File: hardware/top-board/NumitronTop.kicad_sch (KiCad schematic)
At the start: 11 parts, among them J1 61201621621, U1 AP7361C-Y5-13

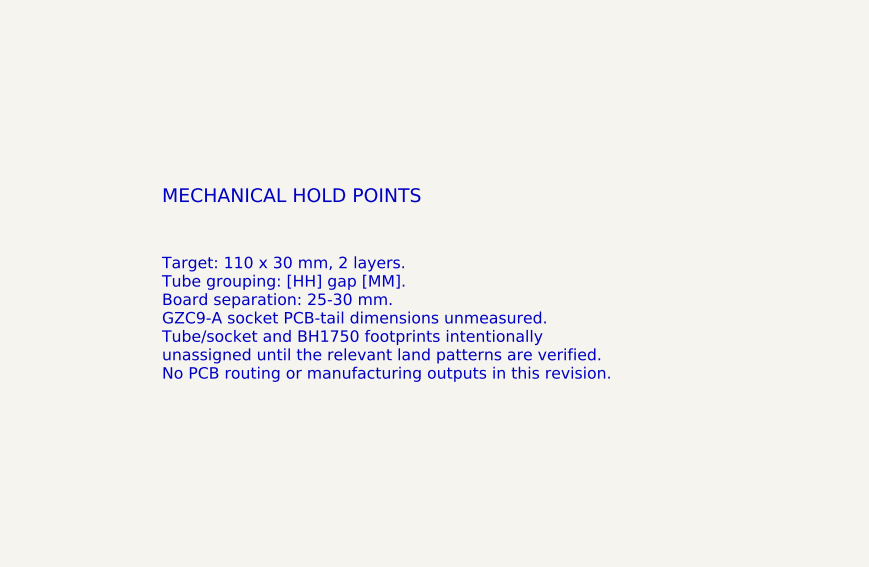
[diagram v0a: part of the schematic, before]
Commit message: Add provisional GZC9-A footprint and unblock top-board placement
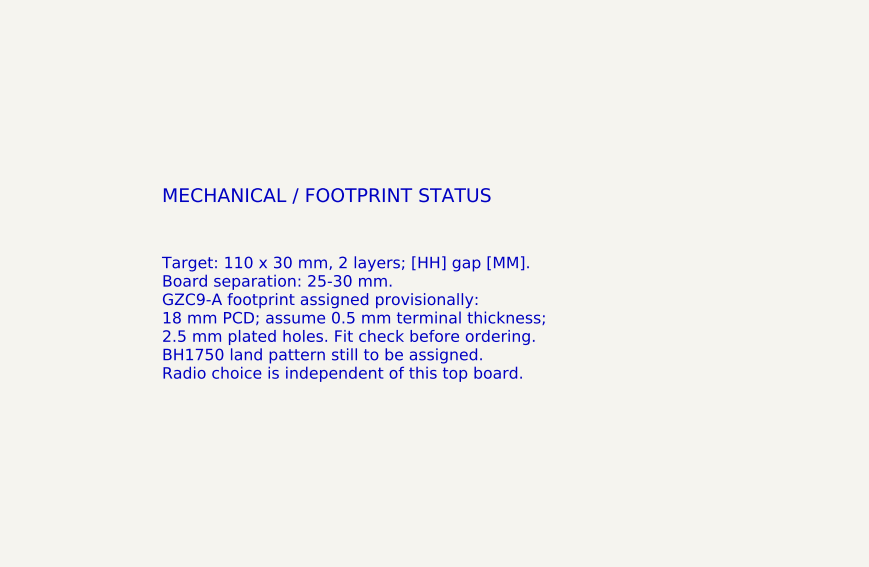
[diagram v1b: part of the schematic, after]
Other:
- note added: "MECHANICAL / FOOTPRINT STATUS"
- note added: "Target: 110 x 30 mm, 2 layers; [HH] gap [MM]. Board separation: 25-30 mm. GZC9-A footprint assigned provisionally: 18 mm PCD; assume 0.5 mm terminal thickness; 2.5 mm plated holes. Fit check before ordering. BH1750 land pattern still to be assigned. Radio choice is independent of this top board."
- note removed: "MECHANICAL HOLD POINTS"
- note removed: "Target: 110 x 30 mm, 2 layers. Tube grouping: [HH] gap [MM]. Board separation: 25-30 mm. GZC9-A socket PCB-tail dimensions unmeasured. Tube/socket and BH1750 footprints intentionally unassigned until the relevant land patterns are verified. No PCB routing or manufacturing outputs in this revision."
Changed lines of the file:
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@@
           (in_bom no) (on_board no) (dnp no)
  (property "Reference" "#FLG004" (at 214.63 152.4 0) (effects (font (size 1.27 1.27)) (justify left) hide))(property "Value" "PWR_FLAG" (at 214.63 154.94 0) (effects (font (size 1.27 1.27)) (justify left) hide))(property "Footprint" "" (at 0 0 0) (effects (font (size 1.27 1.27))  hide))(property "Datasheet" "" (at 0 0 0) (effects (font (size 1.27 1.27))  hide))(property "Description" "External supply declaration for ERC" (at 0 0 0) (effects (font (size 1.27 1.27))  hide)) (pin "1")
-          (instances (project "NumitronTop" (path "/89c4ac53-0d74-5f5d-9ed8-8226c02dc936" (reference "#FLG004") (unit 1)))))(wire (pts (xy 210.82 153.67) (xy 210.82 158.75)) (stroke (width 0.1524) (type default)))(global_label "GND" (shape input) (at 210.82 158.75 0) (effects (font (size 1.016 1.016)) (justify left) ))(text "Bottom board supplies regulated 3.3 V and protected 5 V.\nBudget up to 0.77 A nominal filament load plus logic.\nVerify cold-filament surge, USB current authorization,\nribbon loss, LDO dropout and enclosure temperature.\nNo battery, charging, USB-C or telemetry circuitry here." (at 17.78 171.45 0) (effects (font (size 1.27 1.27)) (justify left top) ))(text "MECHANICAL HOLD POINTS" (at 266.7 145.415 0) (effects (font (size 1.524 1.524)) (justify left top) ))(text "Target: 110 x 30 mm, 2 layers.\nTube grouping: [HH] gap [MM].\nBoard separation: 25-30 mm.\nGZC9-A socket PCB-tail dimensions unmeasured.\nTube/socket and BH1750 footprints intentionally\nunassigned until the relevant land patterns are verified.\nNo PCB routing or manufacturing outputs in this revision." (at 266.7 153.035 0) (effects (font (size 1.27 1.27)) (justify left top) ))(sheet (at 35.56 223.52) (size 76.2 25.4) (fields_autoplaced yes)
+          (instances (project "NumitronTop" (path "/89c4ac53-0d74-5f5d-9ed8-8226c02dc936" (reference "#FLG004") (unit 1)))))(wire (pts (xy 210.82 153.67) (xy 210.82 158.75)) (stroke (width 0.1524) (type default)))(global_label "GND" (shape input) (at 210.82 158.75 0) (effects (font (size 1.016 1.016)) (justify left) ))(text "Bottom board supplies regulated 3.3 V and protected 5 V.\nBudget up to 0.77 A nominal filament load plus logic.\nVerify cold-filament surge, USB current authorization,\nribbon loss, LDO dropout and enclosure temperature.\nNo battery, charging, USB-C or telemetry circuitry here." (at 17.78 171.45 0) (effects (font (size 1.27 1.27)) (justify left top) ))(text "MECHANICAL / FOOTPRINT STATUS" (at 266.7 145.415 0) (effects (font (size 1.524 1.524)) (justify left top) ))(text "Target: 110 x 30 mm, 2 layers; [HH] gap [MM].\nBoard separation: 25-30 mm.\nGZC9-A footprint assigned provisionally:\n18 mm PCD; assume 0.5 mm terminal thickness;\n2.5 mm plated holes. Fit check before ordering.\nBH1750 land pattern still to be assigned.\nRadio choice is independent of this top board." (at 266.7 153.035 0) (effects (font (size 1.27 1.27)) (justify left top) ))(sheet (at 35.56 223.52) (size 76.2 25.4) (fields_autoplaced yes)
          (stroke (width 0.254) (type default)) (fill (color 0 0 0 0))
          (property "Sheetname" "Logic / ambient light" (at 35.56 222.25 0) (effects (font (size 1.27 1.27)) (justify left bottom) ))

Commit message: Complete routed top-board prototype layout
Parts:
- J1: footprint Connector_IDC:IDC-Header_2x08_P2.54mm_Vertical -> Numitron:Wurth_61201621621_2x08_P2.54mm
- U1: footprint Package_TO_SOT_SMD:SOT-89-5 -> Numitron:Diodes_SOT89-5_AP7361C
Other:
- note added: "Working layout: 110 x 40 mm, 2 layers; [HH] gap [MM]. Board separation: 25-30 mm. GZC9-A footprint assigned provisionally: 18 mm PCD; assume 0.5 mm terminal thickness; 2.5 mm plated holes. Fit check before ordering. BH1750: six lands, no soldered center metal. Radio choice is independent of this top board."
- note removed: "Target: 110 x 30 mm, 2 layers; [HH] gap [MM]. Board separation: 25-30 mm. GZC9-A footprint assigned provisionally: 18 mm PCD; assume 0.5 mm terminal thickness; 2.5 mm plated holes. Fit check before ordering. BH1750 land pattern still to be assigned. Radio choice is independent of this top board."
